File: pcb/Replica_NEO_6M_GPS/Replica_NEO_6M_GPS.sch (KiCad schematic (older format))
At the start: 22 parts, among them J1 CONUFL001-SMD-T, J2 Conn_01x04, U1 TPS79133DBVR, U2 NEO-6M-GPS, U3 24AA32A-I_MS

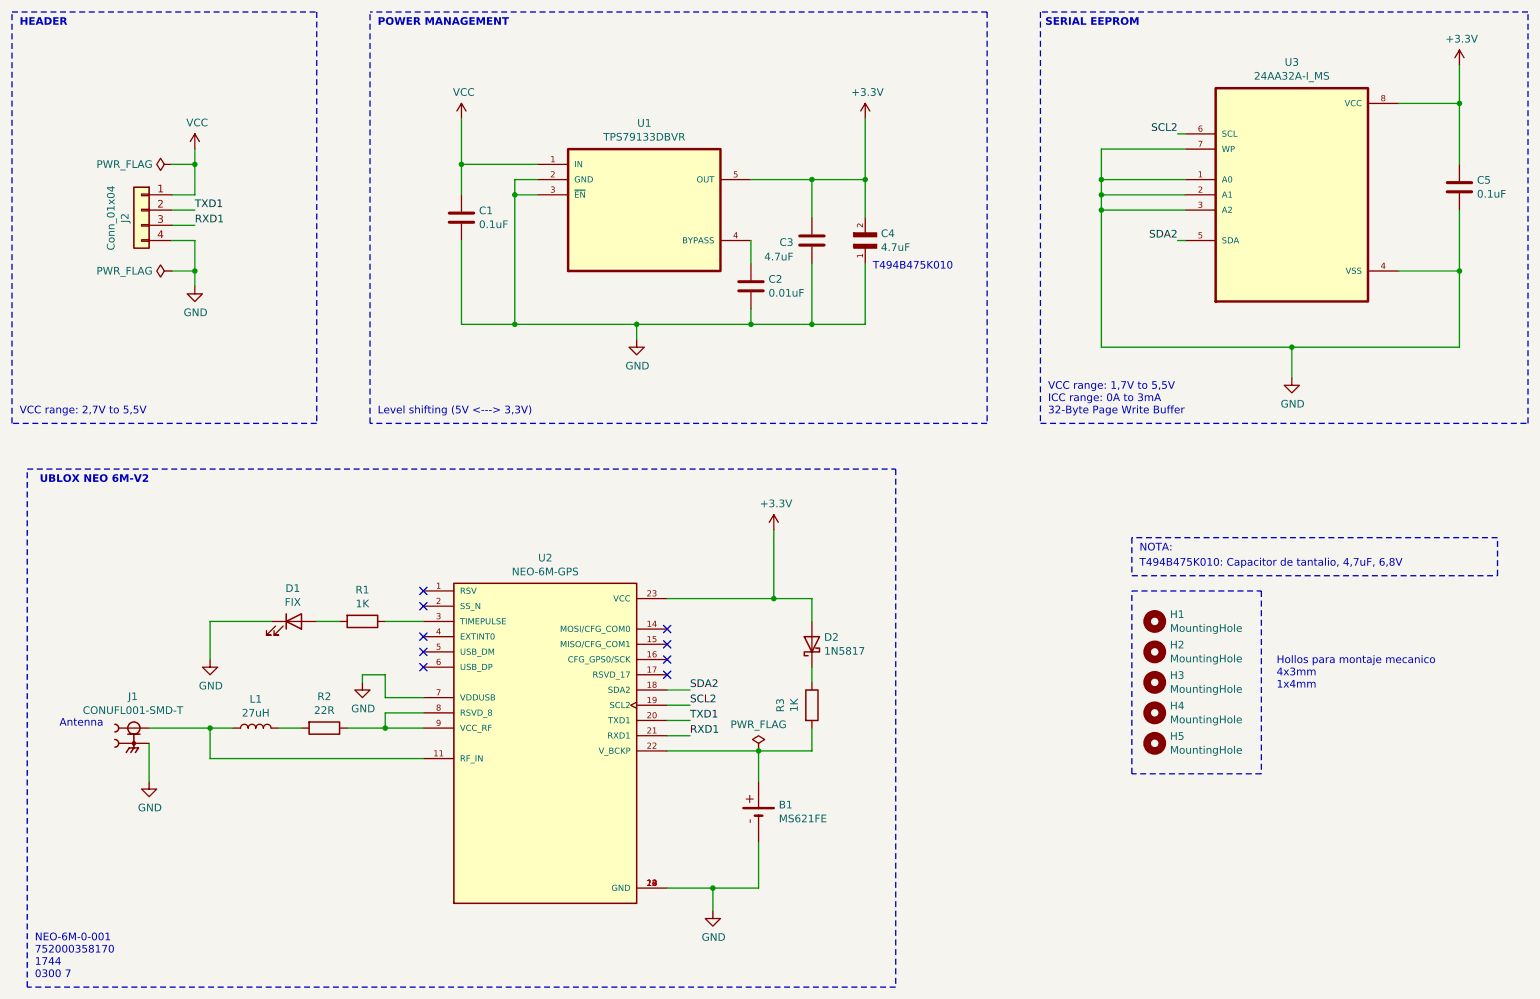
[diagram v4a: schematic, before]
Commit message: Se acomodaron directorios y se hicieron correcciones
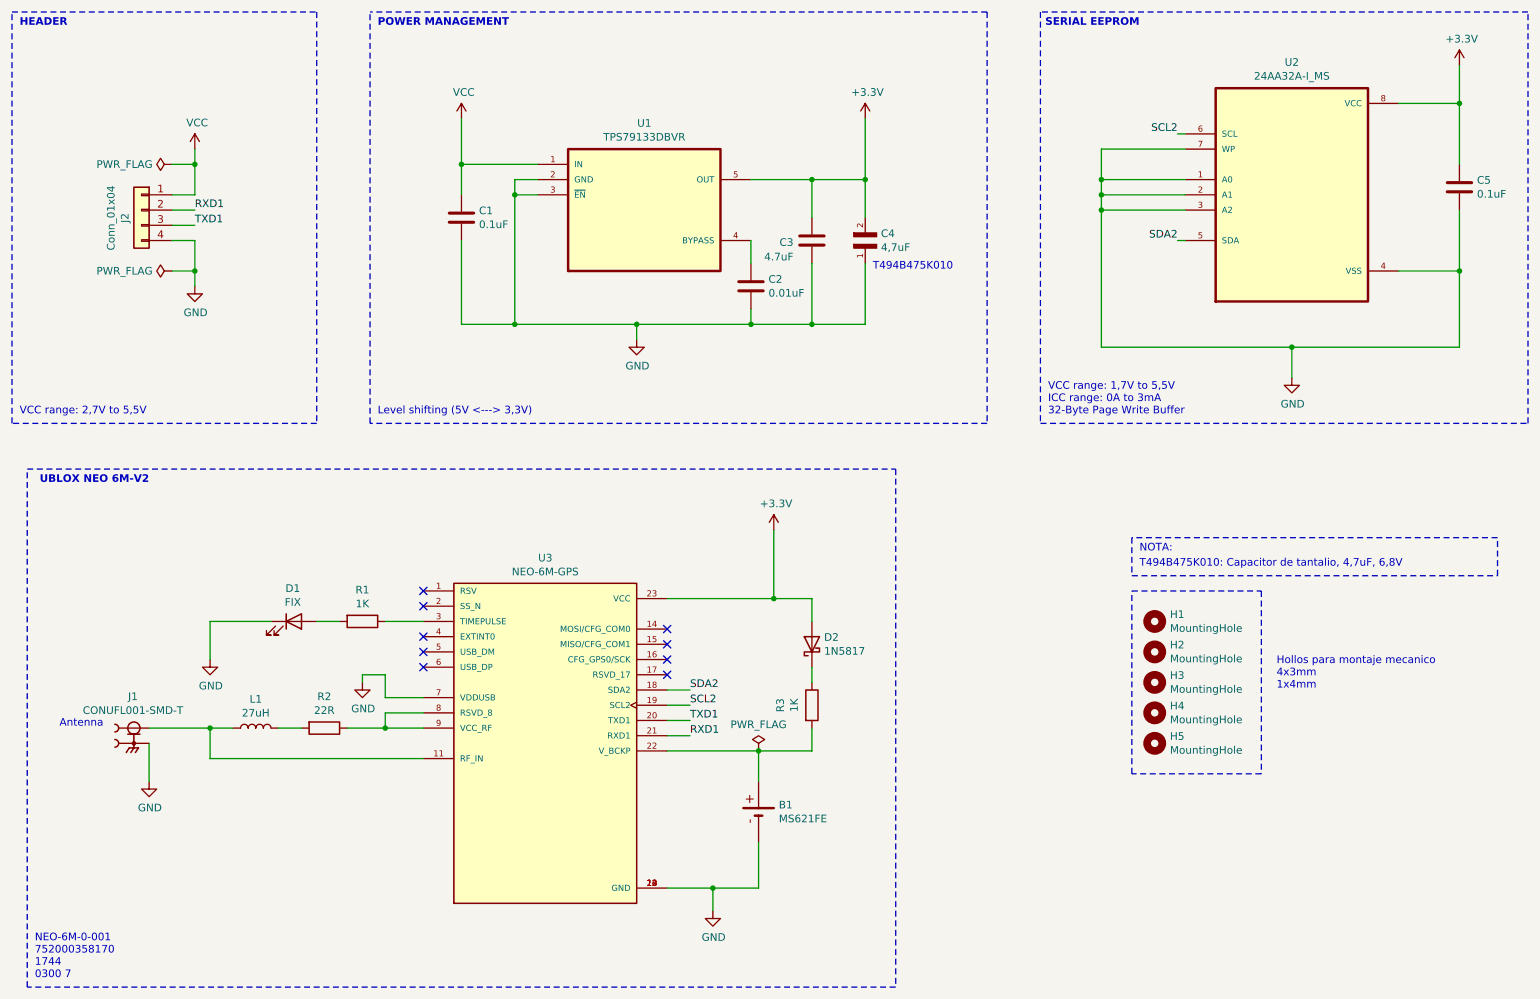
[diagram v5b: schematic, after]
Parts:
- removed J1: CONUFL001-SMD-T, foot:LINX_CONUFL001-SMD-T, symbol Replica_NEO_6M_GPS-rescue:CONUFL001-SMD-T-CONUFL001-SMD-T
- removed U1: TPS79133DBVR, foot:SOT95P280X145-5N, symbol Replica_NEO_6M_GPS-rescue:TPS79133DBVR-TPS79133DBVR
- removed U2: NEO-6M-GPS, foot:XCVR_NEO-6M-GPS, symbol Replica_NEO_6M_GPS-rescue:NEO-6M-GPS-NEO-6M-GPS
- removed U3: 24AA32A-I_MS, foot:SOP65P490X110-8N, symbol Replica_NEO_6M_GPS-rescue:24AA32A-I_MS-24AA32A-I_MS
- added J1: CONUFL001-SMD-T, foot:LINX_CONUFL001-SMD-T, symbol CONUFL001-SMD-T:CONUFL001-SMD-T
- added U1: TPS79133DBVR, foot:SOT95P280X145-5N, symbol TPS79133DBVR:TPS79133DBVR
- added U2: 24AA32A-I_MS, foot:SOP65P490X110-8N, symbol 24AA32A-I_MS:24AA32A-I_MS
- added U3: NEO-6M-GPS, foot:XCVR_NEO-6M-GPS, symbol NEO-6M-GPS:NEO-6M-GPS
- C4: value 4.7uF -> 4,7uF
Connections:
- net +3V3: now also U1.5 (OUT), U2.8 (VCC), U3.23 (VCC)
- net GND: now also J1.2, J1.3, U1.2 (GND), U1.3 (~EN), U2.1 (A0), U2.2 (A1), U2.3 (A2), U2.4 (VSS), U2.7 (WP), U3.10 (GND), U3.12 (GND), U3.13 (GND), U3.24 (GND), U3.7 (VDDUSB)
- net RXD1: now also J2.2 (Pin_2), U3.21 (RXD1); no longer J2.3 (Pin_3)
- net SCL2: now also U2.6 (SCL), U3.19 (SCL2)
- net SDA2: now also U2.5 (SDA), U3.18 (SDA2)
- net TXD1: now also J2.3 (Pin_3), U3.20 (TXD1); no longer J2.2 (Pin_2)
- net VCC: now also U1.1 (IN)
- net at C2.1: now also U1.4 (BYPASS)
- net at L1.1: now also J1.1, U3.11 (RF_IN)
- net at B1.+, R3.2: now also U3.22 (V_BCKP)
- net at R1.1: now also U3.3 (TIMEPULSE)
- net at R2.1: now also U3.8 (RSVD_8), U3.9 (VCC_RF)
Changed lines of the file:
@@
 Hollos para montaje mecanico\n4x3mm\n1x4mm
-$Comp
-L Replica_NEO_6M_GPS-rescue:TPS79133DBVR-TPS79133DBVR U?
-U 1 1 611DC34F
-P 4950 1950
-AR Path="/60EC53CA/611DC34F" Ref="U?"  Part="1"
-AR Path="/611DC34F" Ref="U1"  Part="1"
-F 0 "U1" H 4950 2520 50  0000 C CNN
-F 1 "TPS79133DBVR" H 4950 2429 50  0000 C CNN
-F 2 "foot:SOT95P280X145-5N" H 4950 1950 50  0001 L BNN
-F 3 "" H 4950 1950 50  0001 L BNN
-	1    4950 1950
-	1    0    0    -1
-$EndComp
 $Comp
 L Device:C C?
@@
 	4900 2700 5650 2700
 $Comp
-L Replica_NEO_6M_GPS-rescue:24AA32A-I_MS-24AA32A-I_MS U3
-U 1 1 611DEABD
-P 9200 1850
-AR Path="/611DEABD" Ref="U3"  Part="1"
-AR Path="/60EC55E9/611DEABD" Ref="U?"  Part="1"
-F 0 "U3" H 9200 2720 50  0000 C CNN
-F 1 "24AA32A-I_MS" H 9200 2629 50  0000 C CNN
-F 2 "foot:SOP65P490X110-8N" H 9200 1850 50  0001 L BNN
-F 3 "" H 9200 1850 50  0001 L BNN
-	1    9200 1850
-	1    0    0    -1
-$EndComp
-$Comp
 L Device:C C?
 U 1 1 611DEAC3
@@
 	7950 2850 9200 2850
 $Comp
-L Replica_NEO_6M_GPS-rescue:NEO-6M-GPS-NEO-6M-GPS U2
-U 1 1 612068E8
-P 4300 5400
-F 0 "U2" H 4300 6567 50  0000 C CNN
-F 1 "NEO-6M-GPS" H 4300 6476 50  0000 C CNN
-F 2 "foot:XCVR_NEO-6M-GPS" H 4300 5400 50  0001 L BNN
-F 3 "" H 4300 5400 50  0001 L BNN
-F 4 "R15" H 4300 5400 50  0001 L BNN "PARTREV"
-F 5 "U-Blox" H 4300 5400 50  0001 L BNN "MANUFACTURER"
-F 6 "Manufacturer Recommendations" H 4300 5400 50  0001 L BNN "STANDARD"
-	1    4300 5400
-	1    0    0    -1
-$EndComp
-$Comp
 L Device:R R3
 U 1 1 612068EE
@@
 Wire Wire Line
 	5100 5200 5250 5200
-$Comp
-L Replica_NEO_6M_GPS-rescue:CONUFL001-SMD-T-CONUFL001-SMD-T J1
-U 1 1 61206952
-P 1600 5450
-AR Path="/61206952" Ref="J1"  Part="1"
-AR Path="/60EC55A9/61206952" Ref="J?"  Part="1"
-F 0 "J1" H 1594 5757 50  0000 C CNN
-F 1 "CONUFL001-SMD-T" H 1594 5666 50  0000 C CNN
-F 2 "foot:LINX_CONUFL001-SMD-T" H 1600 5450 50  0001 L BNN
-F 3 "" H 1600 5450 50  0001 L BNN
-F 4 "B" H 1600 5450 50  0001 L BNN "PARTREV"
-F 5 "Linx Technologies" H 1600 5450 50  0001 L BNN "MANUFACTURER"
-F 6 "Manufacturer Recommendations" H 1600 5450 50  0001 L BNN "STANDARD"
-	1    1600 5450
-	1    0    0    -1
-$EndComp
 Wire Wire Line
 	1700 5350 2100 5350
 Wire Wire Line
 	1700 5450 1700 5700
-$Comp
-L MS621FE:MS621FE B1
-U 1 1 61206968
-P 5700 5900
-F 0 "B1" V 5746 5767 50  0000 R CNN
-F 1 "MS621FE" V 5655 5767 50  0000 R CNN
-F 2 "foot:MS621FE" H 5700 5900 50  0001 L BNN
-F 3 "" H 5700 5900 50  0001 L BNN
-	1    5700 5900
-	0    -1   -1   0
-$EndComp
 Wire Notes Line width 12
 	7550 650  7550 3350
@@
 Text Notes 850  3300 0    50   ~ 0
 VCC range: 2,7V to 5,5V
-$Comp
-L Connector_Generic:Conn_01x04 J?
-U 1 1 60FCF122
-P 1650 1950
-AR Path="/60EC55A9/60FCF122" Ref="J?"  Part="1"
-AR Path="/60FCF122" Ref="J2"  Part="1"
-F 0 "J2" V 1758 1898 50  0000 C CNN
-F 1 "Conn_01x04" V 1850 1898 50  0000 C CNN
-F 2 "Connector_PinHeader_2.54mm:PinHeader_1x04_P2.54mm_Horizontal" H 1650 1950 50  0001 C CNN
-F 3 "~" H 1650 1950 50  0001 C CNN
-	1    1650 1950
-	-1   0    0    -1
-$EndComp
 $Comp
 L power:VCC #PWR01
@@
 	1850 2050 2000 2050
 Text Label 2000 1950 0    50   ~ 0
+RXD1
+Text Label 2000 2050 0    50   ~ 0
 TXD1
-Text Label 2000 2050 0    50   ~ 0
-RXD1
 Text Notes 3200 750  0    50   ~ 10
 POWER MANAGEMENT
@@
 	5700 5500 5700 5700
 Wire Wire Line
-	5700 6100 5700 6400
-Wire Wire Line
 	5700 6400 5400 6400
 Connection ~ 5400 6400
@@
 	7950 1550 7950 1750
 Connection ~ 7950 1750
-$Comp
-L TAJP156M006SNJ:TAJP156M006SNJ C4
-U 1 1 615314BE
-P 6400 2100
-F 0 "C4" V 6404 2203 50  0000 L CNN
-F 1 "4.7uF" V 6495 2203 50  0000 L CNN
-F 2 "foot:CAPC2012X140N" H 6400 2100 50  0001 L BNN
-F 3 "" H 6400 2100 50  0001 L BNN
-	1    6400 2100
-	0    1    1    0
-$EndComp
 Text Notes 6450 2350 0    50   ~ 0
 T494B475K010
@@
 Wire Notes Line
 	10550 4100 8150 4100
+$Comp
+L Connector_Generic:Conn_01x04 J?
+U 1 1 60FCF122
+P 1650 1950
+AR Path="/60EC55A9/60FCF122" Ref="J?"  Part="1"
+AR Path="/60FCF122" Ref="J2"  Part="1"
+F 0 "J2" V 1758 1898 50  0000 C CNN
+F 1 "Conn_01x04" V 1850 1898 50  0000 C CNN
+F 2 "Connector_PinHeader_2.54mm:PinHeader_1x04_P2.54mm_Horizontal" H 1650 1950 50  0001 C CNN
+F 3 "~" H 1650 1950 50  0001 C CNN
+	1    1650 1950
+	-1   0    0    -1
+$EndComp
+$Comp
+L 24AA32A-I_MS:24AA32A-I_MS U2
+U 1 1 6120920F
+P 9200 1850
+F 0 "U2" H 9200 2720 50  0000 C CNN
+F 1 "24AA32A-I_MS" H 9200 2629 50  0000 C CNN
+F 2 "foot:SOP65P490X110-8N" H 9200 1850 50  0001 L BNN
+F 3 "" H 9200 1850 50  0001 L BNN
+	1    9200 1850
+	1    0    0    -1
+$EndComp
+$Comp
+L TPS79133DBVR:TPS79133DBVR U1
+U 1 1 6120A40D
+P 4950 1950
+F 0 "U1" H 4950 2520 50  0000 C CNN
+F 1 "TPS79133DBVR" H 4950 2429 50  0000 C CNN
+F 2 "foot:SOT95P280X145-5N" H 4950 1950 50  0001 L BNN
+F 3 "" H 4950 1950 50  0001 L BNN
+	1    4950 1950
+	1    0    0    -1
+$EndComp
+$Comp
+L NEO-6M-GPS:NEO-6M-GPS U3
+U 1 1 6120C054
+P 4300 5400
+F 0 "U3" H 4300 6567 50  0000 C CNN
+F 1 "NEO-6M-GPS" H 4300 6476 50  0000 C CNN
+F 2 "foot:XCVR_NEO-6M-GPS" H 4300 5950 50  0001 L BNN
+F 3 "" H 4300 5400 50  0001 L BNN
+F 4 "R15" H 4300 5400 50  0001 L BNN "PARTREV"
+F 5 "U-Blox" H 4300 5400 50  0001 L BNN "MANUFACTURER"
+F 6 "Manufacturer Recommendations" H 2700 5300 50  0001 L BNN "STANDARD"
+	1    4300 5400
+	1    0    0    -1
+$EndComp
+$Comp
+L CONUFL001-SMD-T:CONUFL001-SMD-T J1
+U 1 1 61213C69
+P 1600 5450
+F 0 "J1" H 1594 5757 50  0000 C CNN
+F 1 "CONUFL001-SMD-T" H 1594 5666 50  0000 C CNN
+F 2 "foot:LINX_CONUFL001-SMD-T" H 1600 5450 50  0001 L BNN
+F 3 "" H 1600 5450 50  0001 L BNN
+F 4 "B" H 1600 5450 50  0001 L BNN "PARTREV"
+F 5 "Linx Technologies" H 1600 5450 50  0001 L BNN "MANUFACTURER"
+F 6 "Manufacturer Recommendations" H 1600 5450 50  0001 L BNN "STANDARD"
+	1    1600 5450
+	1    0    0    -1
+$EndComp
+$Comp
+L TAJP156M006SNJ:TAJP156M006SNJ C4
+U 1 1 6121DBCC
+P 6400 2100
+F 0 "C4" V 6404 2203 50  0000 L CNN
+F 1 "4,7uF" V 6495 2203 50  0000 L CNN
+F 2 "foot:CAPC2012X140N" H 6400 2100 50  0001 L BNN
+F 3 "" H 6400 2100 50  0001 L BNN
+	1    6400 2100
+	0    1    1    0
+$EndComp
+Wire Wire Line
+	5700 6100 5700 6400
+$Comp
+L MS621FE:MS621FE B1
+U 1 1 61206968
+P 5700 5900
+F 0 "B1" V 5746 5767 50  0000 R CNN
+F 1 "MS621FE" V 5655 5767 50  0000 R CNN
+F 2 "foot:MS621FE" H 5700 5900 50  0001 L BNN
+F 3 "" H 5700 5900 50  0001 L BNN
+	1    5700 5900
+	0    -1   -1   0
+$EndComp
 $EndSCHEMATC

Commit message: Se hiceron correcciones 23/08/2021
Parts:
- removed H5: MountingHole, MountingHole:MountingHole_4mm, symbol Mechanical:MountingHole
- added FID1, FID2: Fiducial, Fiducial:Fiducial_0.5mm_Mask1mm, symbol Mechanical:Fiducial
- added H6, H7, H8, H9: MountingHole, MountingHole:MountingHole_3.5mm_Pad, symbol Mechanical:MountingHole
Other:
- note added: "Fiduciales"
- note added: "Hollos para montaje mecanico\n4x3mm\n"
- note added: "Pads rectangulares para fijacion del modulo"
- note removed: "Hollos para montaje mecanico\n4x3mm\n1x4mm"
- moved on the sheet: H1, H2, H3, H4
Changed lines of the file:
@@
 L Mechanical:MountingHole H1
 U 1 1 61193E6F
-P 8300 4650
-F 0 "H1" H 8400 4696 50  0000 L CNN
-F 1 "MountingHole" H 8400 4605 50  0000 L CNN
-F 2 "MountingHole:MountingHole_3mm" H 8300 4650 50  0001 C CNN
-F 3 "~" H 8300 4650 50  0001 C CNN
-	1    8300 4650
+P 7750 4050
+F 0 "H1" H 7850 4096 50  0000 L CNN
+F 1 "MountingHole" H 7850 4005 50  0000 L CNN
+F 2 "MountingHole:MountingHole_3mm" H 7750 4050 50  0001 C CNN
+F 3 "~" H 7750 4050 50  0001 C CNN
+	1    7750 4050
 	1    0    0    -1
 $EndComp
@@
 L Mechanical:MountingHole H2
 U 1 1 611942D8
-P 8300 4850
-F 0 "H2" H 8400 4896 50  0000 L CNN
-F 1 "MountingHole" H 8400 4805 50  0000 L CNN
-F 2 "MountingHole:MountingHole_3mm" H 8300 4850 50  0001 C CNN
-F 3 "~" H 8300 4850 50  0001 C CNN
-	1    8300 4850
+P 7750 4250
+F 0 "H2" H 7850 4296 50  0000 L CNN
+F 1 "MountingHole" H 7850 4205 50  0000 L CNN
+F 2 "MountingHole:MountingHole_3mm" H 7750 4250 50  0001 C CNN
+F 3 "~" H 7750 4250 50  0001 C CNN
+	1    7750 4250
 	1    0    0    -1
 $EndComp
@@
 L Mechanical:MountingHole H3
 U 1 1 6119459C
-P 8300 5050
-F 0 "H3" H 8400 5096 50  0000 L CNN
-F 1 "MountingHole" H 8400 5005 50  0000 L CNN
-F 2 "MountingHole:MountingHole_3mm" H 8300 5050 50  0001 C CNN
-F 3 "~" H 8300 5050 50  0001 C CNN
-	1    8300 5050
+P 7750 4450
+F 0 "H3" H 7850 4496 50  0000 L CNN
+F 1 "MountingHole" H 7850 4405 50  0000 L CNN
+F 2 "MountingHole:MountingHole_3mm" H 7750 4450 50  0001 C CNN
+F 3 "~" H 7750 4450 50  0001 C CNN
+	1    7750 4450
 	1    0    0    -1
 $EndComp
@@
 L Mechanical:MountingHole H4
 U 1 1 611948E2
-P 8300 5250
-F 0 "H4" H 8400 5296 50  0000 L CNN
-F 1 "MountingHole" H 8400 5205 50  0000 L CNN
-F 2 "MountingHole:MountingHole_3mm" H 8300 5250 50  0001 C CNN
-F 3 "~" H 8300 5250 50  0001 C CNN
-	1    8300 5250
-	1    0    0    -1
-$EndComp
-$Comp
-L Mechanical:MountingHole H5
-U 1 1 611961F1
-P 8300 5450
-F 0 "H5" H 8400 5496 50  0000 L CNN
-F 1 "MountingHole" H 8400 5405 50  0000 L CNN
-F 2 "MountingHole:MountingHole_4mm" H 8300 5450 50  0001 C CNN
-F 3 "~" H 8300 5450 50  0001 C CNN
-	1    8300 5450
-	1    0    0    -1
-$EndComp
-Wire Notes Line
-	8150 4450 9000 4450
-Wire Notes Line
-	9000 5650 8150 5650
-Wire Notes Line
-	8150 5650 8150 4450
-Wire Notes Line
-	9000 4450 9000 5650
-Text Notes 9100 5100 0    50   ~ 0
-Hollos para montaje mecanico\n4x3mm\n1x4mm
+P 7750 4650
+F 0 "H4" H 7850 4696 50  0000 L CNN
+F 1 "MountingHole" H 7850 4605 50  0000 L CNN
+F 2 "MountingHole:MountingHole_3mm" H 7750 4650 50  0001 C CNN
+F 3 "~" H 7750 4650 50  0001 C CNN
+	1    7750 4650
+	1    0    0    -1
+$EndComp
+Wire Notes Line
+	8450 4800 7600 4800
+Text Notes 8550 4500 0    50   ~ 0
+Hollos para montaje mecanico\n4x3mm\n
 $Comp
 L Device:C C?
@@
 Text Notes 950  7000 0    50   ~ 0
 NEO-6M-0-001\n752000358170\n1744\n0300 7
-Text Notes 8200 4300 0    50   ~ 0
+Text Notes 7650 3750 0    50   ~ 0
 T494B475K010: Capacitor de tantalio, 4,7uF, 6,8V
-Text Notes 8200 4200 0    50   ~ 0
+Text Notes 7650 3650 0    50   ~ 0
 NOTA:
 Wire Notes Line
-	8150 4100 8150 4350
-Wire Notes Line
-	8150 4350 10550 4350
-Wire Notes Line
-	10550 4350 10550 4100
-Wire Notes Line
-	10550 4100 8150 4100
+	7600 3550 7600 3800
+Wire Notes Line
+	7600 3800 10000 3800
+Wire Notes Line
+	10000 3800 10000 3550
+Wire Notes Line
+	10000 3550 7600 3550
 $Comp
 L Connector_Generic:Conn_01x04 J?
@@
 	0    -1   -1   0
 $EndComp
+Text Notes 8550 5400 0    50   ~ 0
+Pads rectangulares para fijacion del modulo
+$Comp
+L Mechanical:MountingHole H6
+U 1 1 6126C73C
+P 7750 5050
+F 0 "H6" H 7850 5096 50  0000 L CNN
+F 1 "MountingHole" H 7850 5005 50  0000 L CNN
+F 2 "MountingHole:MountingHole_3.5mm_Pad" H 7750 5050 50  0001 C CNN
+F 3 "~" H 7750 5050 50  0001 C CNN
+	1    7750 5050
+	1    0    0    -1
+$EndComp
+$Comp
+L Mechanical:MountingHole H7
+U 1 1 6126CD10
+P 7750 5250
+F 0 "H7" H 7850 5296 50  0000 L CNN
+F 1 "MountingHole" H 7850 5205 50  0000 L CNN
+F 2 "MountingHole:MountingHole_3.5mm_Pad" H 7750 5250 50  0001 C CNN
+F 3 "~" H 7750 5250 50  0001 C CNN
+	1    7750 5250
+	1    0    0    -1
+$EndComp
+$Comp
+L Mechanical:MountingHole H8
+U 1 1 6126D3BC
+P 7750 5450
+F 0 "H8" H 7850 5496 50  0000 L CNN
+F 1 "MountingHole" H 7850 5405 50  0000 L CNN
+F 2 "MountingHole:MountingHole_3.5mm_Pad" H 7750 5450 50  0001 C CNN
+F 3 "~" H 7750 5450 50  0001 C CNN
+	1    7750 5450
+	1    0    0    -1
+$EndComp
+$Comp
+L Mechanical:MountingHole H9
+U 1 1 6126D990
+P 7750 5650
+F 0 "H9" H 7850 5696 50  0000 L CNN
+F 1 "MountingHole" H 7850 5605 50  0000 L CNN
+F 2 "MountingHole:MountingHole_3.5mm_Pad" H 7750 5650 50  0001 C CNN
+F 3 "~" H 7750 5650 50  0001 C CNN
+	1    7750 5650
+	1    0    0    -1
+$EndComp
+Wire Notes Line
+	7600 4900 8450 4900
+$Comp
+L Mechanical:Fiducial FID1
+U 1 1 612CAD4A
+P 7750 6050
+F 0 "FID1" H 7835 6096 50  0000 L CNN
+F 1 "Fiducial" H 7835 6005 50  0000 L CNN
+F 2 "Fiducial:Fiducial_0.5mm_Mask1mm" H 7750 6050 50  0001 C CNN
+F 3 "~" H 7750 6050 50  0001 C CNN
+	1    7750 6050
+	1    0    0    -1
+$EndComp
+$Comp
+L Mechanical:Fiducial FID2
+U 1 1 612CB3A8
+P 7750 6250
+F 0 "FID2" H 7835 6296 50  0000 L CNN
+F 1 "Fiducial" H 7835 6205 50  0000 L CNN
+F 2 "Fiducial:Fiducial_0.5mm_Mask1mm" H 7750 6250 50  0001 C CNN
+F 3 "~" H 7750 6250 50  0001 C CNN
+	1    7750 6250
+	1    0    0    -1
+$EndComp
+Wire Notes Line
+	7600 5800 8450 5800
+Wire Notes Line
+	8450 5800 8450 4900
+Wire Notes Line
+	7600 4900 7600 5800
+Wire Notes Line
+	7600 5900 8450 5900
+Wire Notes Line
+	8450 5900 8450 6400
+Wire Notes Line
+	8450 6400 7600 6400
+Wire Notes Line
+	7600 6400 7600 5900
+Wire Notes Line
+	7600 4800 7600 3900
+Wire Notes Line
+	8450 3900 8450 4800
+Wire Notes Line
+	7600 3900 8450 3900
+Text Notes 8550 6150 0    50   ~ 0
+Fiduciales
 $EndSCHEMATC
